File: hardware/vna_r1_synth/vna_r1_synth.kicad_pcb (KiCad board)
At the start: 2 copper layers, 119 parts, among them J301 Conn_02x10_Odd_Even, Q301 Q_PMOS_DGS, U201 LMX2594, U301 CONN_SMA_2GND, U302 CONN_SMA_2GND, U303 LM27762, U304 74HC244, U305 74LVC1G32, U401 LTC2630-LZ8, U402 MAAM-011100, U403 ADRF5020, U404 LTC2054CS5, U501 CONN_SMA_2GND, U502 CONN_SMA_2GND, U503 CONN_SMA_2GND, U504 CONN_SMA_2GND, U505 CONN_SMA_2GND, U902 ADP7158

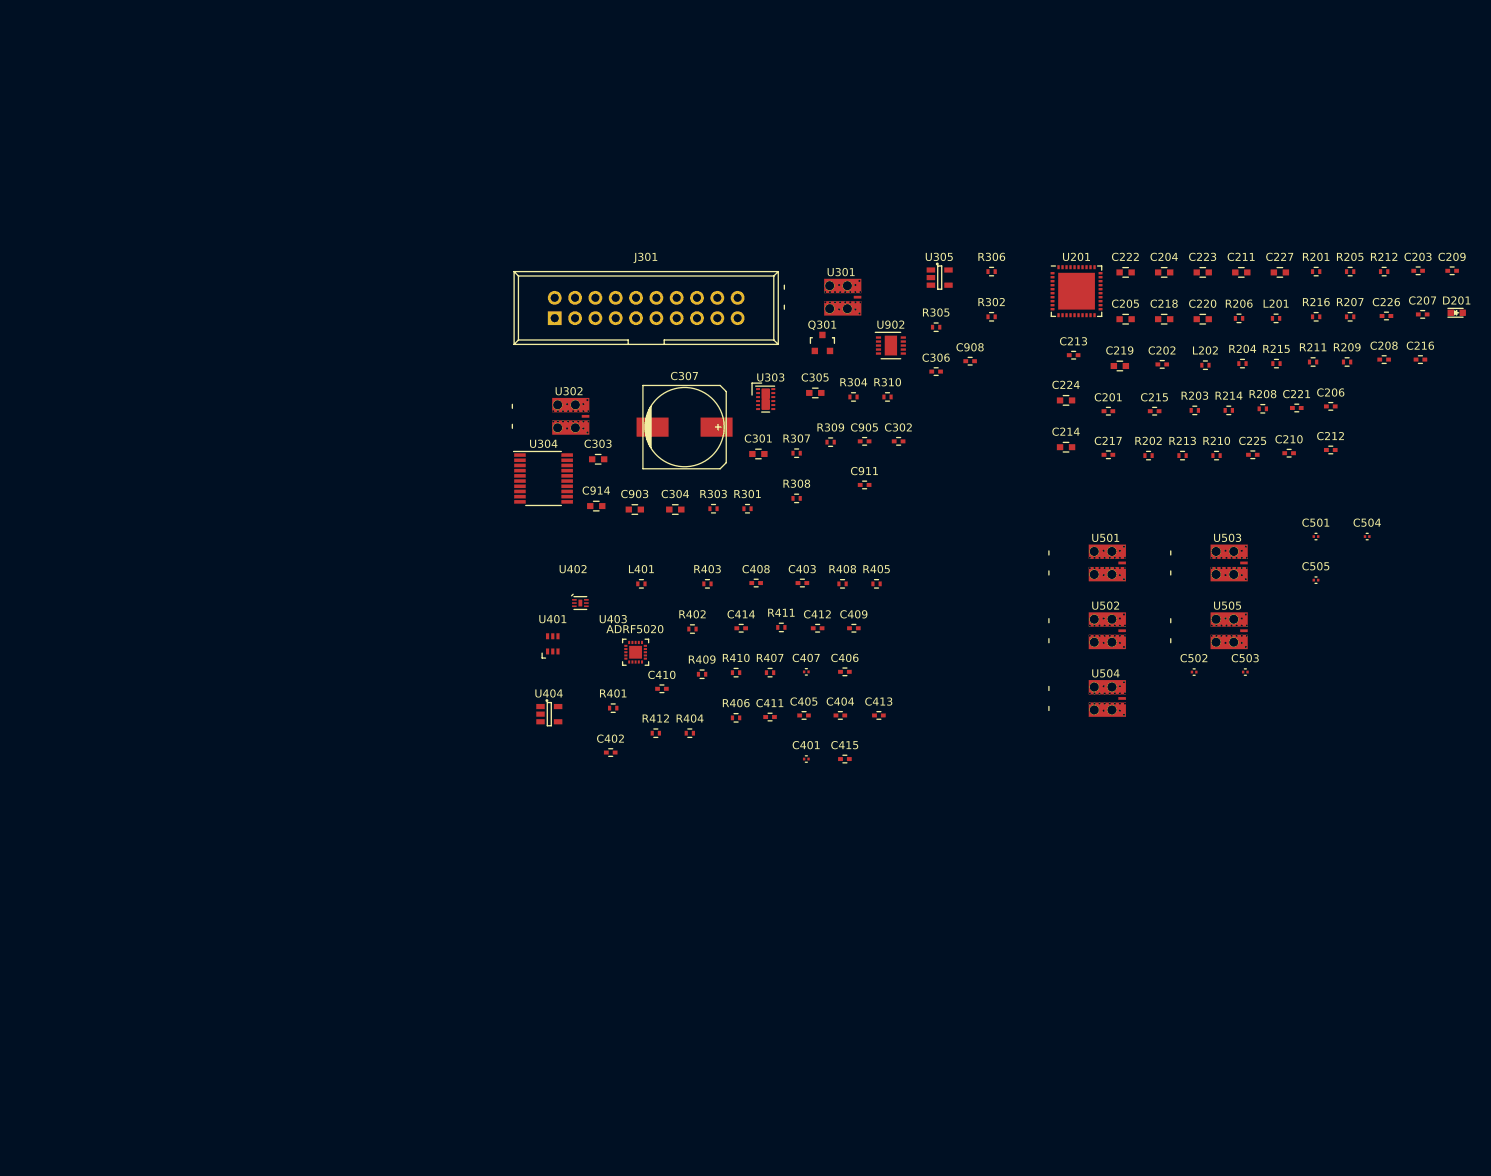
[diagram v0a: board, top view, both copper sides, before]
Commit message: component placement on vna r1 demod and synth
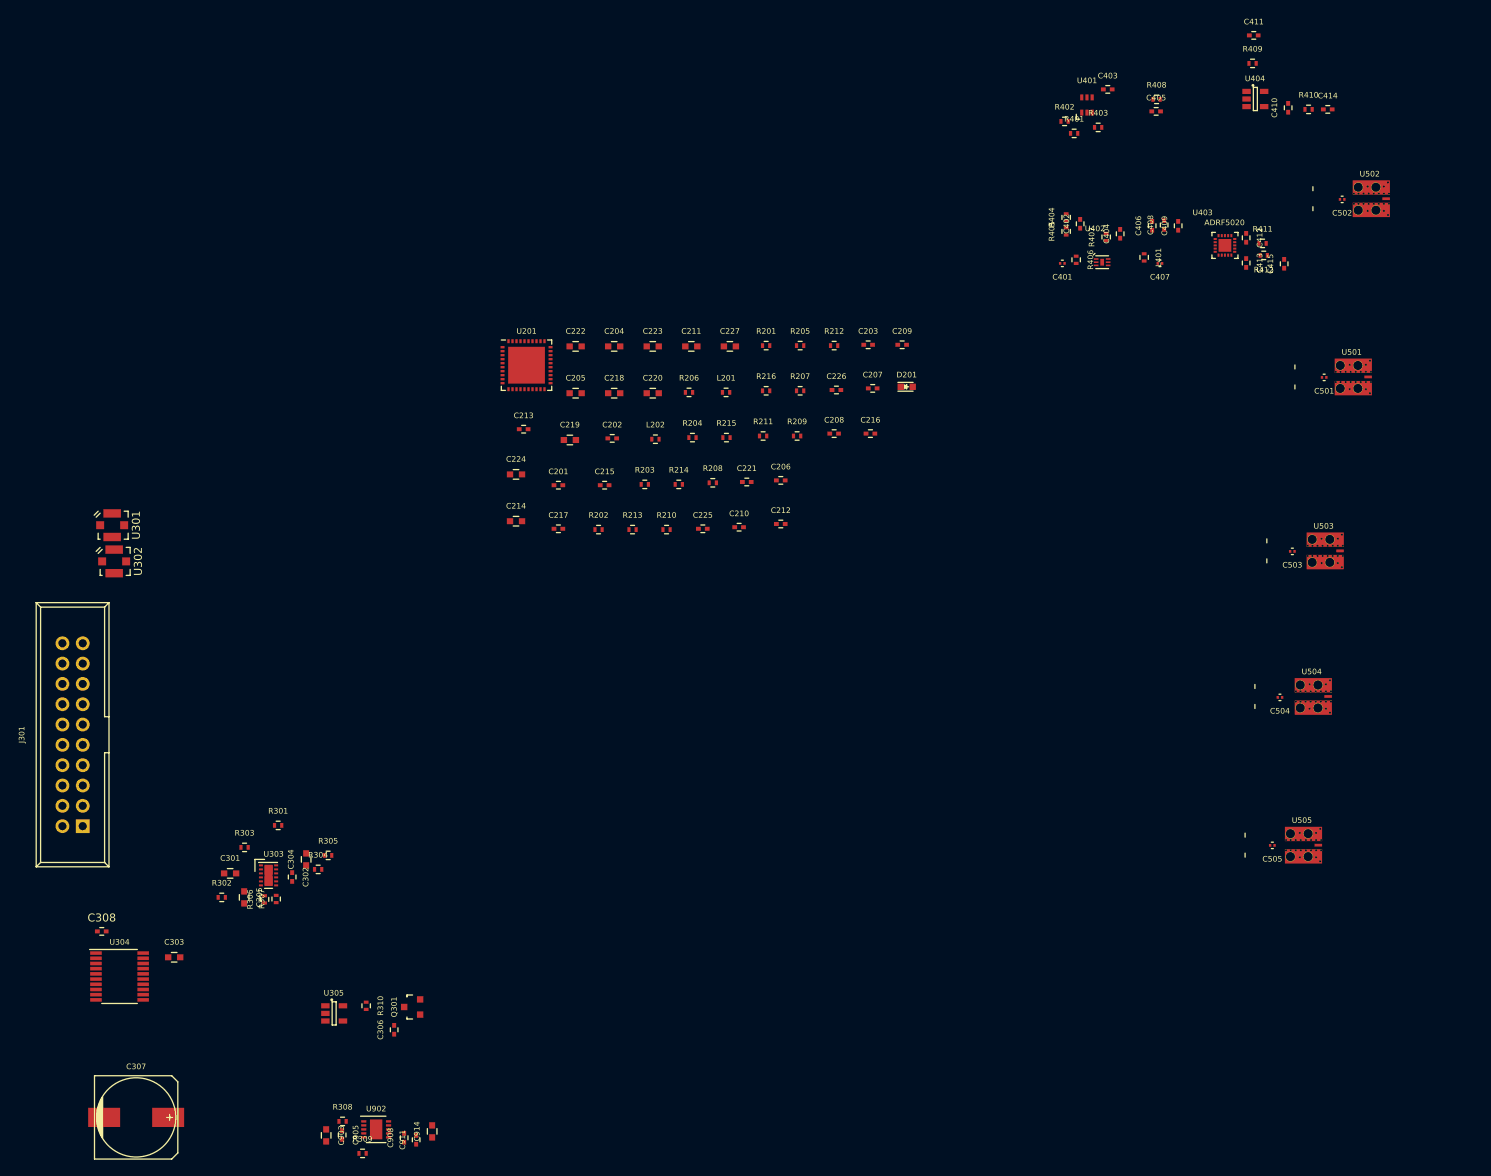
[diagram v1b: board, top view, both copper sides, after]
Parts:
- added C308: 1 uF, Capacitors_SMD:C_0402, F.Cu at (39.5, 155.5)
- U301, U302: footprint vna_footprints:SMA_901-10512_6p7MIL_FR408_CPW_LAUNCH -> vna_footprints:734120110_ufl_umc
- moved R302 120.5 mm to (54.5, 151.2)
- moved C908 120.1 mm to (77.2, 181.3), turned to 90 degrees
- moved R306 120.1 mm to (59.8, 151.5), turned to 90 degrees
- moved U305 119.1 mm to (68.5, 165.8)
- moved U902 117.2 mm to (73.8, 180.2)
- moved U404 117.1 mm to (183.7, 51.5)
- moved C307 110.2 mm to (43.8, 178.8)
- moved C905 108.5 mm to (69.5, 180.9), turned to 270 degrees
- moved C410 106.8 mm to (187.8, 52.5), turned to 90 degrees
- moved C306 106.6 mm to (76.0, 167.8), turned to 90 degrees
- moved R309 106.4 mm to (72.0, 183.2)
- moved C411 104.5 mm to (183.4, 43.5)
- moved R409 102.8 mm to (183.3, 47.0)
- moved R305 100.7 mm to (67.8, 146.0)
- moved R410 100.4 mm to (190.3, 52.8)
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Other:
- copper layers 2 -> 4
- rule pad_to_mask_clearance: 0.2 -> 0.05

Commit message: layout on r1
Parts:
- added H301: MOUNTING_HOLE, Mounting_Holes:MountingHole_2-5mm, F.Cu at (41.5, 146.8)
- added H302: MOUNTING_HOLE, Mounting_Holes:MountingHole_2-5mm, F.Cu at (40.8, 104.0)
- added H303: MOUNTING_HOLE, Mounting_Holes:MountingHole_2-5mm, F.Cu at (100.0, 105.0)
- added H304: MOUNTING_HOLE, Mounting_Holes:MountingHole_2-5mm, F.Cu at (99.5, 142.0)
- added H305: MOUNTING_HOLE, Mounting_Holes:MountingHole_2-5mm, F.Cu at (134.0, 98.8)
- added H306: MOUNTING_HOLE, Mounting_Holes:MountingHole_2-5mm, F.Cu at (44.2, 90.0)
- added R217: DNP, Resistors_SMD:R_0402, F.Cu at (77.0, 125.2)
- C307: footprint Capacitors_SMD:c_elec_10x10 -> Capacitors_SMD:c_elec_6.3x5.8
- moved R410 111.0 mm to (92.5, 105.2)
- moved R409 110.7 mm to (86.5, 100.8)
- moved U404 110.7 mm to (86.9, 105.2)
- moved C414 110.5 mm to (94.7, 103.8)
- moved C410 110.2 mm to (90.8, 104.8)
- moved C411 108.7 mm to (91.7, 101.8)
- moved R408 104.7 mm to (80.5, 103.8)
- moved C405 104.7 mm to (80.5, 105.2)
- moved C403 100.7 mm to (79.0, 102.2)
- moved R401 99.8 mm to (74.8, 106.0)
- moved R402 99.8 mm to (73.5, 104.5)
- moved R403 99.8 mm to (77.8, 105.2)
- moved U401 99.8 mm to (76.3, 102.4)
- moved U502 92.9 mm to (113.5, 102.0)
- moved C502 92.7 mm to (110.0, 102.0)
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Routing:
- net GND: track 0.00 -> 17.4 mm
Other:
- board outline added: 89 x 57.2 mm

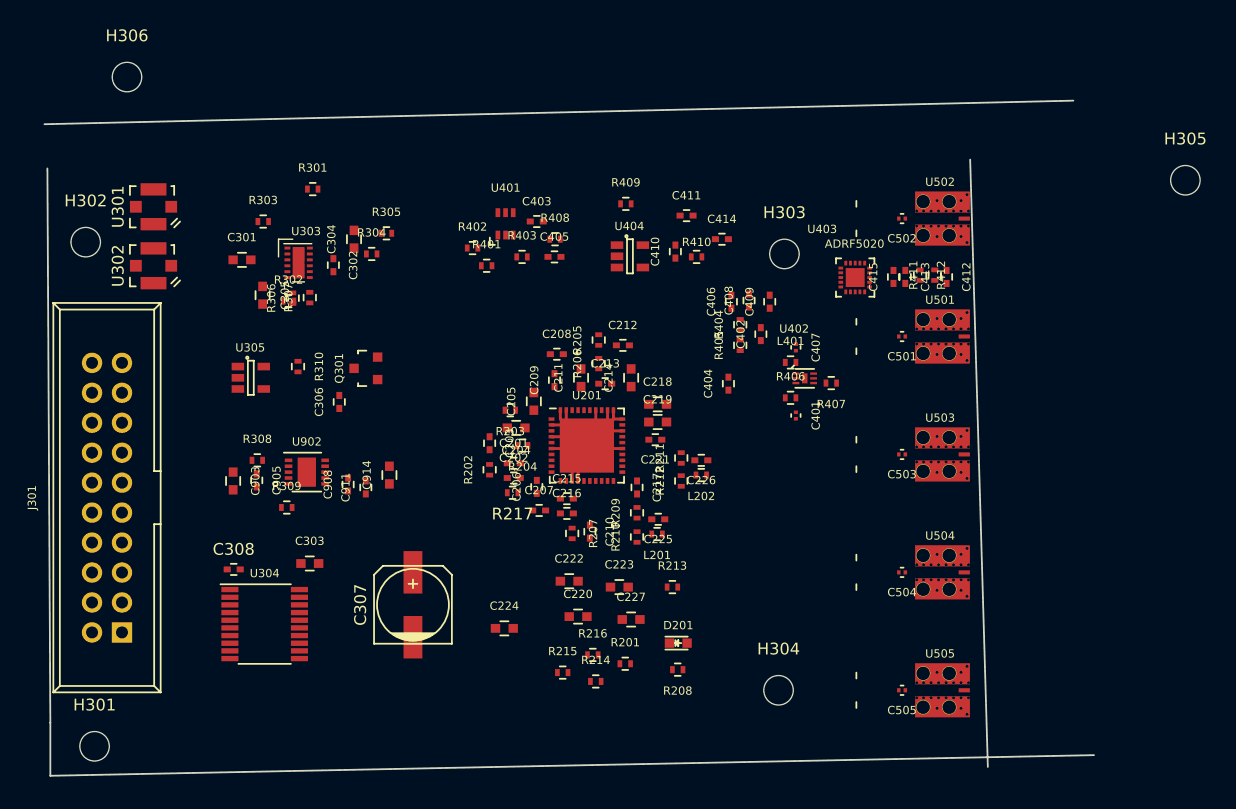
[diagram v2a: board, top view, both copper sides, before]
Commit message: all nets connected on vna synth r1
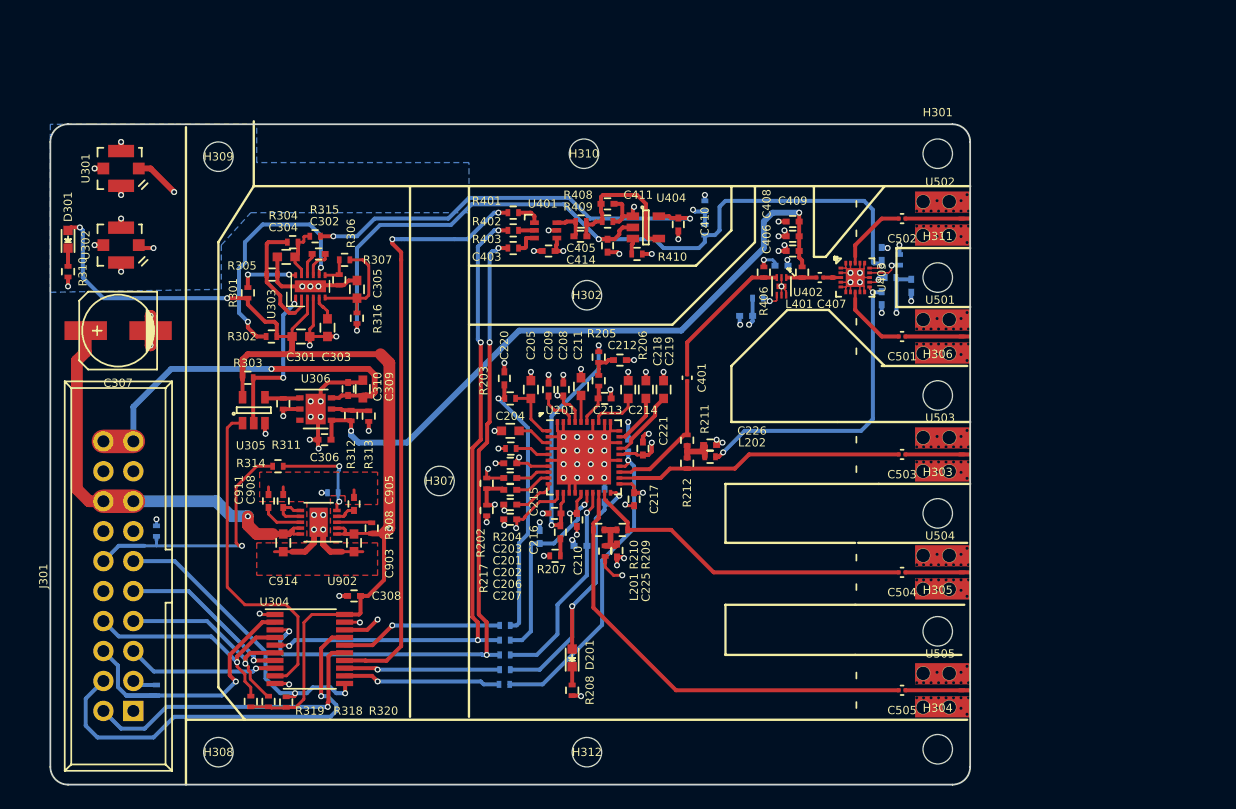
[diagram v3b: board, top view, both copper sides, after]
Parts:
- removed Q301: Q_PMOS_DGS, TO_SOT_Packages_SMD:SOT-23
- added C309: 2.2 uF, Capacitors_SMD:C_0603, F.Cu at (64.2, 116.5)
- added C310: 100 nF, Capacitors_SMD:C_0402, F.Cu at (63.0, 116.5)
- added D301: RED, LEDs:LED_0603, F.Cu at (39.2, 103.8)
- added H307: MOUNTING_HOLE, Mounting_Holes:MountingHole_2-5mm, F.Cu at (70.8, 124.2)
- added H308: MOUNTING_HOLE, Mounting_Holes:MountingHole_2-5mm, F.Cu at (52.0, 147.2)
- added H309: MOUNTING_HOLE, Mounting_Holes:MountingHole_2-5mm, F.Cu at (52.0, 96.8)
- added H310: MOUNTING_HOLE, Mounting_Holes:MountingHole_2-5mm, F.Cu at (83.0, 96.5)
- added H311: MOUNTING_HOLE, Mounting_Holes:MountingHole_2-5mm, F.Cu at (113.0, 107.0)
- added H312: MOUNTING_HOLE, Mounting_Holes:MountingHole_2-5mm, F.Cu at (83.2, 147.2)
- added R311: 10k, Resistors_SMD:R_0402, F.Cu at (57.5, 117.7)
- added R312: 10k, Resistors_SMD:R_0402, F.Cu at (63.2, 118.7)
- added R313: 47k, Resistors_SMD:R_0402, F.Cu at (64.8, 118.8)
- added R314: 1k, Resistors_SMD:R_0402, F.Cu at (57.0, 123.0)
- added R315: JMP, Resistors_SMD:R_0402, F.Cu at (60.2, 103.5)
- added R316: JMP, Resistors_SMD:R_0402, F.Cu at (63.8, 110.5)
- added R317: 10k, Resistors_SMD:R_0402, B.Cu at (46.8, 128.5)
- added R318: 10k, Resistors_SMD:R_0402, F.Cu at (56.2, 142.9)
- added R319: 10k, Resistors_SMD:R_0402, F.Cu at (54.8, 142.9)
- added R320: 10k, Resistors_SMD:R_0402, F.Cu at (57.8, 143.0)
- added R321: 10k, Resistors_SMD:R_0402, B.Cu at (46.8, 142.0)
- added U306: LD39100, Housings_DFN_QFN:DFN-6-1EP_3x3mm_Pitch0.95mm, F.Cu at (60.2, 118.2)
- C220: footprint Capacitors_SMD:C_0603 -> Capacitors_SMD:C_0402
- C222, C223, C224, C227: footprint Capacitors_SMD:C_0603 -> Capacitors_SMD:C_0402; moved to B.Cu
- C306: value 1 uF -> 2.2 uF
- C402, C404, C412, C413, C415, R201, R213, R214, R215, R216, R309, R404, R405, R407, R411, R412: moved to B.Cu
- R310: value 1k -> 10k
- moved H301 87.4 mm to (113.0, 96.5)
- moved H306 73.9 mm to (113.0, 117.0)
- moved H305 43.6 mm to (113.0, 137.0)
- moved H302 42.7 mm to (83.2, 108.5)
- moved C307 34.1 mm to (43.5, 111.5), turned to 180 degrees
- moved H303 25.6 mm to (113.0, 127.0)
- moved C220 21.1 mm to (76.2, 115.5), turned to 90 degrees
- moved R310 21.1 mm to (39.2, 106.5), turned to 90 degrees
- moved C303 20.1 mm to (61.2, 111.2), turned to 90 degrees
- moved R213 16.5 mm to (76.2, 141.5), turned to 180 degrees
- moved C227 14.8 mm to (86.8, 121.2), turned to 90 degrees
- moved H304 14.4 mm to (113.0, 147.0)
- moved C224 14.1 mm to (84.8, 125.5), turned to 90 degrees
- moved R303 13.3 mm to (54.5, 115.5), turned to 180 degrees
- moved C903 11.5 mm to (63.5, 129.5), turned to 90 degrees
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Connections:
- C220 pad 1: /conn_power/LMX_CE -> /synth/CE
- C222 pad 1: /SCK -> /synth/SCK
- C223 pad 1: /SDI -> /synth/SDI
- C224 pad 1: /conn_power/LMX_LCK -> /synth/MUXout
- C227 pad 1: /conn_power/LMX_CS -> /synth/CSB
- C304 pad 2: +2V5 -> Net-(C304-Pad2)
- C305 pad 1: -2V5 -> Net-(C305-Pad1)
- D201 pad 2: /conn_power/LMX_LCK -> /synth/MUXout
- J301 pad 11: (no net) -> /conn_power/~AMP_EN_EXT
- J301 pad 19: (no net) -> +5V
- J301 pad 20: (no net) -> +5V
- R201 pad 1: /conn_power/LMX_LCK -> /synth/MUXout
- R203 pad 2: /conn_power/LMX_CE -> /synth/CE
- R213 pad 1: /conn_power/LMX_CS -> /synth/CSB
- R214 pad 1: /SDI -> /synth/SDI
- R214 pad 2: /SDI -> /SPI_SDI
- R215 pad 1: /SCK -> /synth/SCK
- R215 pad 2: /SCK -> /SPI_SCK
- R216 pad 1: /conn_power/LMX_CE -> /synth/CE
- R304 pad 2: +2V5 -> Net-(C304-Pad2)
- R307 pad 1: -2V5 -> Net-(C305-Pad1)
- R309 pad 2: /conn_power/3V3_DEMOD_ENABLE -> Net-(R309-Pad2)
- R310 pad 1: +3V3 -> GND
- R310 pad 2: Net-(Q301-Pad2) -> Net-(D301-Pad1)
- R402 pad 2: /SCK -> /SPI_SCK
- R403 pad 2: /SDI -> /SPI_SDI
- U201 pad 16: /SCK -> /synth/SCK
- U201 pad 17: /SDI -> /synth/SDI
- U201 pad 20: /conn_power/LMX_LCK -> /synth/MUXout
- U201 pad 24: /conn_power/LMX_CS -> /synth/CSB
- U303 pad 11: +2V5 -> Net-(C304-Pad2)
- U303 pad 6: -2V5 -> Net-(C305-Pad1)
- U304 pad 1: (no net) -> GND
- U304 pad 11: (no net) -> /conn_power/~AMP_EN_EXT
- U304 pad 19: (no net) -> GND
- U304 pad 3: /SDI -> /SPI_SDI
- U304 pad 5: /SCK -> /SPI_SCK
- U304 pad 9: +3V3 -> /conn_power/~AMP_EN
- U305 pad 1: +3V3 -> /conn_power/~AMP_EN
- U305 pad 4: Net-(Q301-Pad2) -> Net-(R311-Pad1)
- U902 pad 5: /conn_power/3V3_DEMOD_ENABLE -> Net-(R309-Pad2)
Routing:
- net +3V3: track 0.00 -> 163.9 mm, vias 0 -> 13
- net GND: track 17.4 -> 117.1 mm, vias 0 -> 100
- net /PORT_SEL: track 0.00 -> 74.2 mm, vias 0 -> 2
- net -2V5: track 0.00 -> 68.3 mm, vias 0 -> 3
- net /conn_power/SYNTH_REF_N: track 0.00 -> 59.4 mm, vias 0 -> 2
- net /SPI_SDI: track 0.00 -> 58.4 mm, vias 0 -> 4
- net /AMP_VD: track 0.00 -> 56.9 mm, vias 0 -> 2
- net /SPI_SCK: track 0.00 -> 56.4 mm, vias 0 -> 4
- net /conn_power/SYNTH_REF_P: track 0.00 -> 56.2 mm, vias 0 -> 2
- net /DAC_CS: track 0.00 -> 50.9 mm, vias 0 -> 2
- net /LO_PORT2: track 0.00 -> 38.7 mm
- net +2V5: track 0.00 -> 36.2 mm, vias 0 -> 2
- net VPP: track 0.00 -> 35.9 mm, vias 0 -> 1
- net /conn_power/SDI_EXT: track 0.00 -> 35.5 mm, vias 0 -> 1
- net +5V: track 0.00 -> 32.8 mm, vias 0 -> 1
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- added copper zone on In2.Cu, net +3V3
- added copper zone on B.Cu, net GND
- added copper zone on F.Cu, net GND
- added copper zone on In1.Cu, net GND
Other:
- board size 89 x 57.2 mm -> 78 x 56 mm
- net class Default: clearance 0.2 -> 0.1254; via_dia 0.6 -> 0.51; via_drill 0.4 -> 0.3
- rule trace_clearance: 0.2 -> 0.1254
- rule trace_min: 0.2 -> 0.13
